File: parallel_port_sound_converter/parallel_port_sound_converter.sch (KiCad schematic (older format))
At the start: 16 parts, among them J1 DB25_Male, J2 DB25_Female, U1 LM78L05_TO92, U2 ATtiny2313A-PU

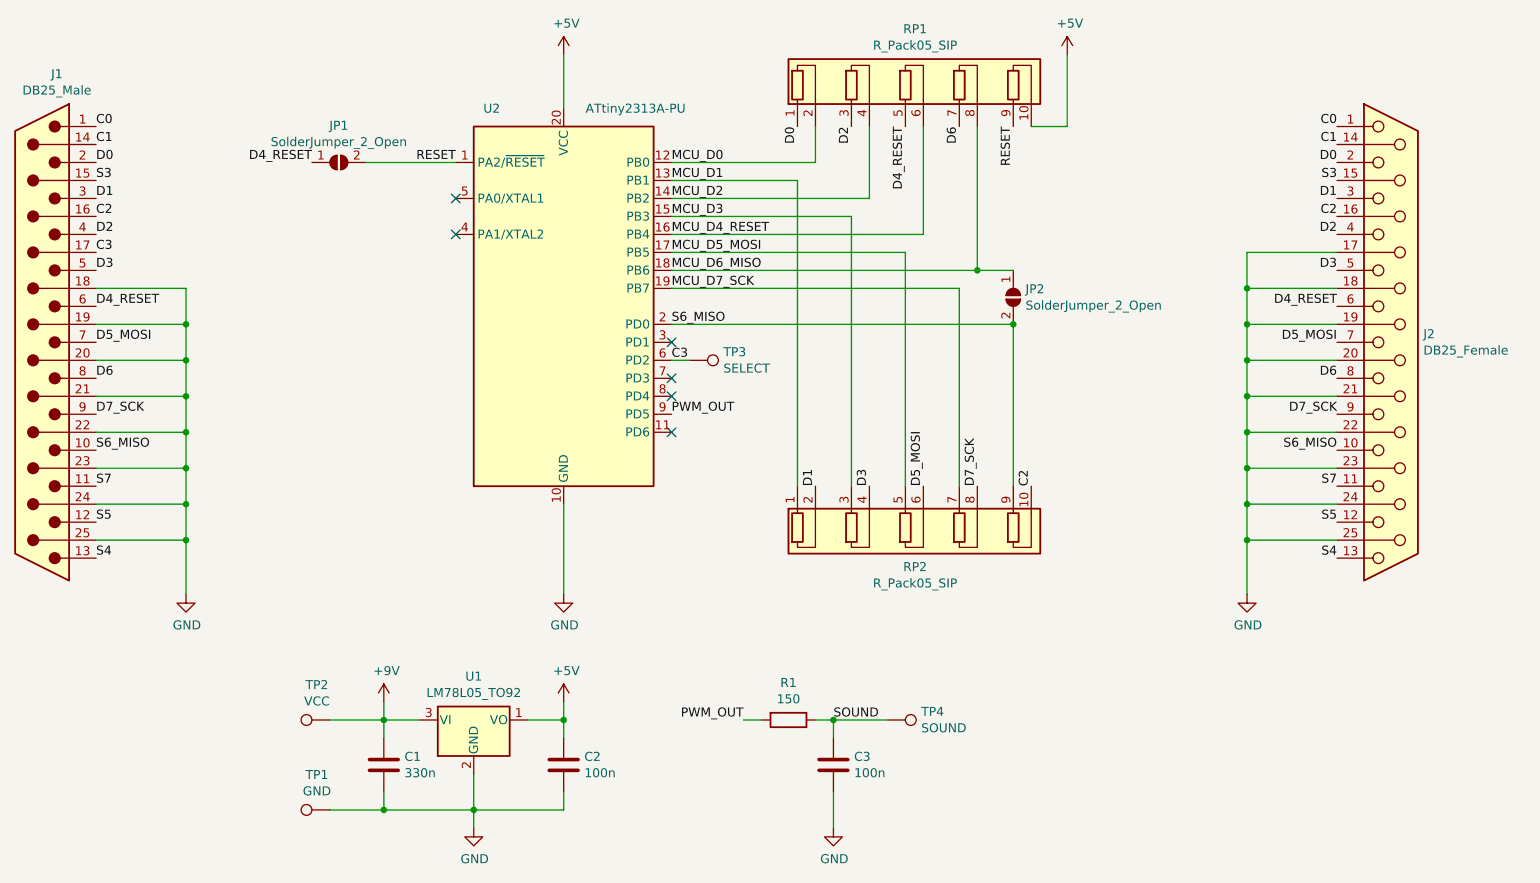
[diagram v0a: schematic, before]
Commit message: switch to ATtiny24
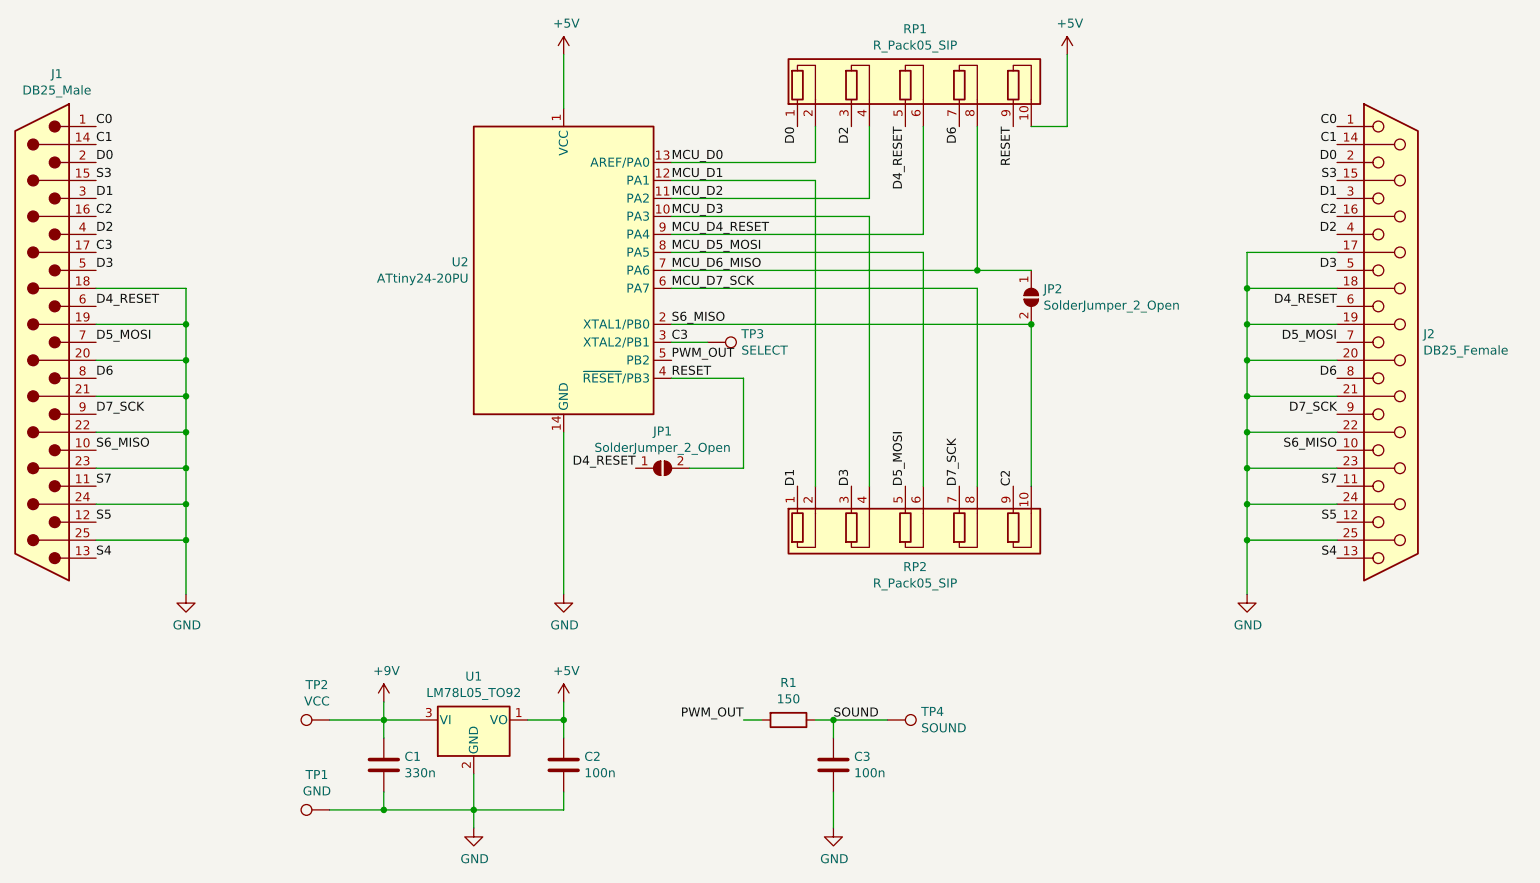
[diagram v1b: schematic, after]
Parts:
- removed U2: ATtiny2313A-PU, Package_DIP:DIP-20_W7.62mm, symbol MCU_Microchip_ATtiny:ATtiny2313A-PU
- added U2: ATtiny24-20PU, Package_DIP:DIP-14_W7.62mm, symbol MCU_Microchip_ATtiny:ATtiny24-20PU
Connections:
- net +5V: now also U2.1 (VCC)
- net C2: now also RP2.9 (R5.1); no longer RP2.10 (R5.2)
- net C3: now also U2.3 (XTAL2/PB1)
- net D1: now also RP2.1 (R1.1); no longer RP2.2 (R1.2)
- net D3: now also RP2.3 (R2.1); no longer RP2.4 (R2.2)
- net D5_MOSI: now also RP2.5 (R3.1); no longer RP2.6 (R3.2)
- net D7_SCK: now also RP2.7 (R4.1); no longer RP2.8 (R4.2)
- net GND: now also U2.14 (GND)
- net MCU_D0: now also U2.13 (AREF/PA0)
- net MCU_D1: now also RP2.2 (R1.2), U2.12 (PA1); no longer RP2.1 (R1.1)
- net MCU_D2: now also U2.11 (PA2)
- net MCU_D3: now also RP2.4 (R2.2), U2.10 (PA3); no longer RP2.3 (R2.1)
- net MCU_D4_RESET: now also U2.9 (PA4)
- net MCU_D5_MOSI: now also RP2.6 (R3.2), U2.8 (PA5); no longer RP2.5 (R3.1)
- net MCU_D6_MISO: now also U2.7 (PA6)
- net MCU_D7_SCK: now also RP2.8 (R4.2), U2.6 (PA7); no longer RP2.7 (R4.1)
- net PWM_OUT: now also U2.5 (PB2)
- net RESET: now also U2.4 (~RESET~/PB3)
- net S6_MISO: now also RP2.10 (R5.2), U2.2 (XTAL1/PB0); no longer RP2.9 (R5.1)
- no-connect marks 6 -> 0
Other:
- moved on the sheet: JP1, JP2, TP3
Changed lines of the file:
@@
 encoding utf-8
 Sheet 1 1
-Title ""
-Date ""
+Title "Parallel Port Sound Converter"
+Date "2019-08-06"
 Rev ""
-Comp ""
+Comp "Benedikt Freisen"
 Comment1 ""
 Comment2 ""
@@
 Text Label 1900 4200 0    50   ~ 0
 S6_MISO
-$Comp
-L MCU_Microchip_ATtiny:ATtiny2313A-PU U2
-U 1 1 5D44B533
-P 4500 3400
-F 0 "U2" H 4100 4500 50  0000 C CNN
-F 1 "ATtiny2313A-PU" H 4900 4500 50  0000 C CNN
-F 2 "Package_DIP:DIP-20_W7.62mm" H 4500 3400 50  0001 C CIN
-F 3 "http://ww1.microchip.com/downloads/en/DeviceDoc/doc8246.pdf" H 4500 3400 50  0001 C CNN
-	1    4500 3400
-	1    0    0    -1
-$EndComp
 Text Label 5100 2600 0    50   ~ 0
 MCU_D0
@@
 L Jumper:SolderJumper_2_Open JP1
 U 1 1 5D4561F9
-P 3250 2600
-F 0 "JP1" H 3250 2805 50  0000 C CNN
-F 1 "SolderJumper_2_Open" H 3250 2714 50  0000 C CNN
-F 2 "Jumper:SolderJumper-2_P1.3mm_Open_RoundedPad1.0x1.5mm" H 3250 2600 50  0001 C CNN
-F 3 "~" H 3250 2600 50  0001 C CNN
-	1    3250 2600
-	1    0    0    -1
-$EndComp
-Text Label 3100 2600 2    50   ~ 0
+P 5050 4300
+F 0 "JP1" H 5050 4505 50  0000 C CNN
+F 1 "SolderJumper_2_Open" H 5050 4414 50  0000 C CNN
+F 2 "Jumper:SolderJumper-2_P1.3mm_Open_RoundedPad1.0x1.5mm" H 5050 4300 50  0001 C CNN
+F 3 "~" H 5050 4300 50  0001 C CNN
+	1    5050 4300
+	1    0    0    -1
+$EndComp
+Text Label 4900 4300 2    50   ~ 0
 D4_RESET
 Wire Wire Line
-	3400 2600 3900 2600
+	5200 4300 5500 4300
 Text Label 5100 3100 0    50   ~ 0
 MCU_D5_MOSI
@@
 	6800 3200 5100 3200
 Wire Wire Line
-	5800 4400 5800 2700
-Wire Wire Line
-	5800 2700 5100 2700
-Wire Wire Line
-	6100 4400 6100 2900
-Wire Wire Line
-	6100 2900 5100 2900
-Wire Wire Line
-	6400 4400 6400 3100
-Wire Wire Line
-	6400 3100 5100 3100
-Wire Wire Line
-	6700 4400 6700 3300
-Wire Wire Line
-	6700 3300 5100 3300
+	5900 4400 5900 2700
+Wire Wire Line
+	6200 4400 6200 2900
+Wire Wire Line
+	6500 4400 6500 3100
+Wire Wire Line
+	6800 4400 6800 3300
 Text Label 5800 2400 3    50   ~ 0
 D0
@@
 Text Label 6700 2400 3    50   ~ 0
 D6
-Text Label 5900 4400 1    50   ~ 0
+Text Label 5800 4400 1    50   ~ 0
 D1
-Text Label 6200 4400 1    50   ~ 0
+Text Label 6100 4400 1    50   ~ 0
 D3
-Text Label 6500 4400 1    50   ~ 0
+Text Label 6400 4400 1    50   ~ 0
 D5_MOSI
-Text Label 6800 4400 1    50   ~ 0
+Text Label 6700 4400 1    50   ~ 0
 D7_SCK
 Wire Wire Line
 	4500 2000 4500 2300
 Wire Wire Line
-	4500 5000 4500 4500
-Wire Wire Line
-	5100 3500 7000 3500
-Wire Wire Line
-	7000 3500 7000 4400
+	7100 3500 7100 4400
 Text Label 5100 3500 0    50   ~ 0
 S6_MISO
@@
 L Jumper:SolderJumper_2_Open JP2
 U 1 1 5D46C1F1
-P 7000 3350
-F 0 "JP2" V 6954 3418 50  0000 L CNN
-F 1 "SolderJumper_2_Open" V 7045 3418 50  0000 L CNN
-F 2 "Jumper:SolderJumper-2_P1.3mm_Open_RoundedPad1.0x1.5mm" H 7000 3350 50  0001 C CNN
-F 3 "~" H 7000 3350 50  0001 C CNN
-	1    7000 3350
+P 7100 3350
+F 0 "JP2" V 7054 3418 50  0000 L CNN
+F 1 "SolderJumper_2_Open" V 7145 3418 50  0000 L CNN
+F 2 "Jumper:SolderJumper-2_P1.3mm_Open_RoundedPad1.0x1.5mm" H 7100 3350 50  0001 C CNN
+F 3 "~" H 7100 3350 50  0001 C CNN
+	1    7100 3350
 	0    1    1    0
 $EndComp
-Connection ~ 7000 3500
-Wire Wire Line
-	6800 3200 7000 3200
 Connection ~ 6800 3200
-Text Label 3900 2600 2    50   ~ 0
+Text Label 5100 3800 0    50   ~ 0
 RESET
 Text Label 7000 2400 3    50   ~ 0
@@
 Wire Wire Line
 	7300 2400 7100 2400
-Text Label 5100 4000 0    50   ~ 0
+Text Label 5100 3700 0    50   ~ 0
 PWM_OUT
-Text Label 5100 3700 0    50   ~ 0
+Text Label 5100 3600 0    50   ~ 0
 C3
 Text Label 8800 2600 2    50   ~ 0
@@
 Text Label 8800 4800 2    50   ~ 0
 S4
-NoConn ~ 3900 2800
-NoConn ~ 3900 3000
-NoConn ~ 5100 3600
-NoConn ~ 5100 3800
-NoConn ~ 5100 3900
-NoConn ~ 5100 4100
-Text Label 7100 4400 1    50   ~ 0
+Text Label 7000 4400 1    50   ~ 0
 C2
 Wire Wire Line
@@
 L Connector:TestPoint TP3
 U 1 1 5D4A0448
-P 5200 3700
-F 0 "TP3" V 5154 3888 50  0000 L CNN
-F 1 "SELECT" V 5245 3888 50  0000 L CNN
-F 2 "Connector_Wire:SolderWirePad_1x01_Drill0.8mm" H 5400 3700 50  0001 C CNN
-F 3 "~" H 5400 3700 50  0001 C CNN
-	1    5200 3700
+P 5300 3600
+F 0 "TP3" V 5254 3788 50  0000 L CNN
+F 1 "SELECT" V 5345 3788 50  0000 L CNN
+F 2 "Connector_Wire:SolderWirePad_1x01_Drill0.8mm" H 5500 3600 50  0001 C CNN
+F 3 "~" H 5500 3600 50  0001 C CNN
+	1    5300 3600
 	0    1    1    0
 $EndComp
@@
 	6300 5700 6000 5700
 Connection ~ 6000 5700
-Wire Wire Line
-	5200 3700 5100 3700
 $Comp
 L Connector:TestPoint TP2
@@
 Wire Wire Line
 	3500 6200 4000 6200
+$Comp
+L MCU_Microchip_ATtiny:ATtiny24-20PU U2
+U 1 1 5D49B950
+P 4500 3200
+F 0 "U2" H 3971 3246 50  0000 R CNN
+F 1 "ATtiny24-20PU" H 3971 3155 50  0000 R CNN
+F 2 "Package_DIP:DIP-14_W7.62mm" H 4500 3200 50  0001 C CIN
+F 3 "http://ww1.microchip.com/downloads/en/DeviceDoc/doc8006.pdf" H 4500 3200 50  0001 C CNN
+	1    4500 3200
+	1    0    0    -1
+$EndComp
+Wire Wire Line
+	4500 4100 4500 5000
+Wire Wire Line
+	5100 3600 5300 3600
+Wire Wire Line
+	5100 3800 5500 3800
+Wire Wire Line
+	5500 3800 5500 4300
+Wire Wire Line
+	5100 2700 5900 2700
+Wire Wire Line
+	5100 2900 6200 2900
+Wire Wire Line
+	5100 3100 6500 3100
+Wire Wire Line
+	5100 3300 6800 3300
+Wire Wire Line
+	6800 3200 7100 3200
+Wire Wire Line
+	5100 3500 7100 3500
+Connection ~ 7100 3500
 $EndSCHEMATC

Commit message: update schematic symbol
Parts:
- U2: symbol MCU_Microchip_ATtiny:ATtiny24-20PU -> parallel_port_sound_converter-rescue:ATtiny24-20PU-MCU_Microchip_ATtiny
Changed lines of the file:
@@
 EESchema Schematic File Version 4
-LIBS:parallel_port_sound_converter-cache
-EELAYER 29 0
+EELAYER 30 0
 EELAYER END
 $Descr A4 11693 8268
@@
 	3500 6200 4000 6200
 $Comp
-L MCU_Microchip_ATtiny:ATtiny24-20PU U2
+L parallel_port_sound_converter-rescue:ATtiny24-20PU-MCU_Microchip_ATtiny U2
 U 1 1 5D49B950
 P 4500 3200
